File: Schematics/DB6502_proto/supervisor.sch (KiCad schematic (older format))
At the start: 33 parts, among them J4 AVR ISP, J5 Debug UART, J6 USB_B, U13 74AC74, U14 ATmega644PA-PU, U15 74HC595, U16 74HC157, U17 FT230XS, U5 74AC04, U7 74HC74, U8 74AC08, Y1 20MHz

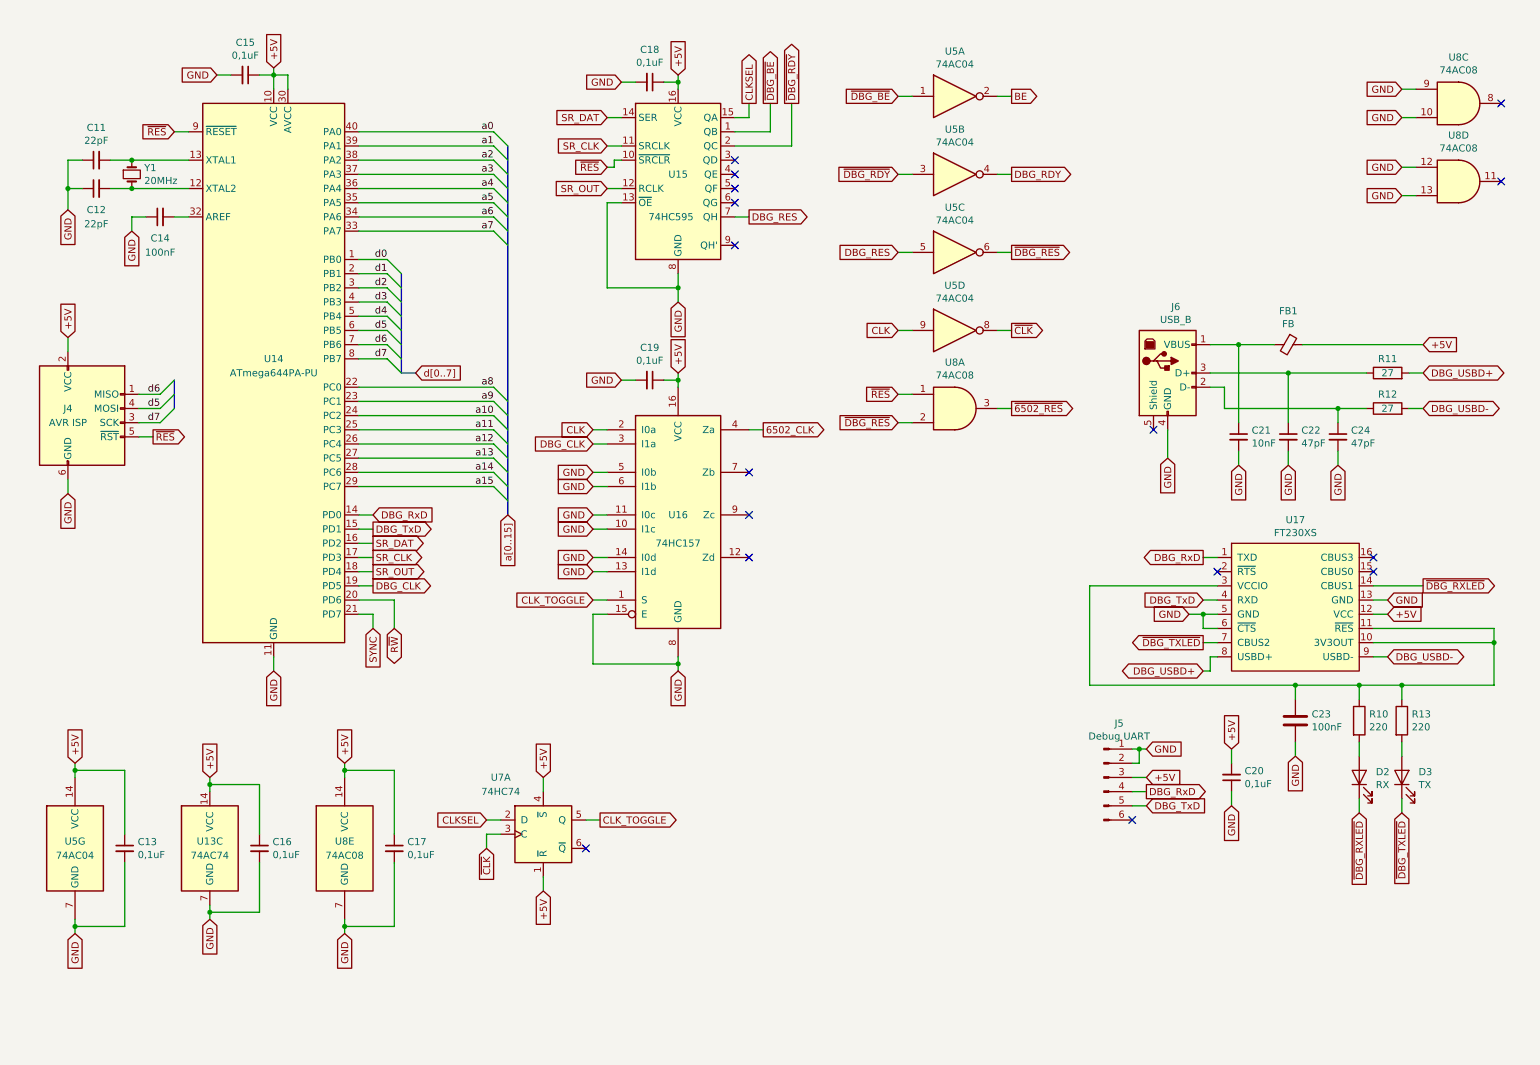
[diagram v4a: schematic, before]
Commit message: Implemented fix for metastability issue during clock switch
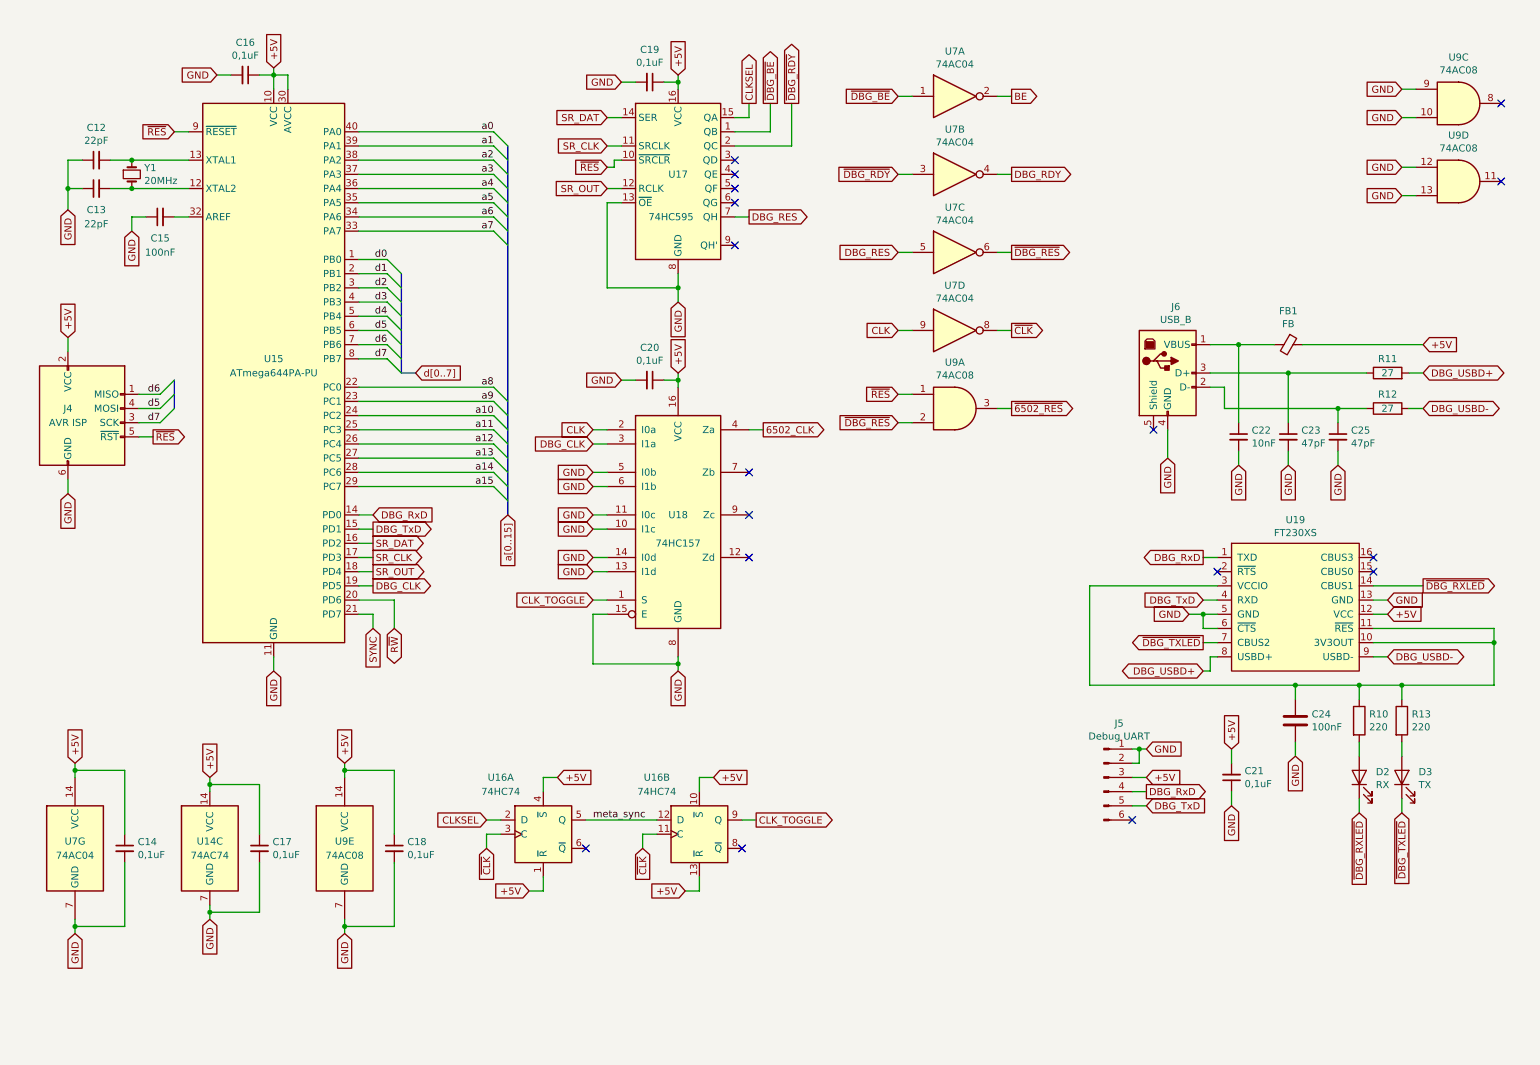
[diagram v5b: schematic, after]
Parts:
- added unit 2 of U16
- renumbered C11 to C12, C12 to C13, C13 to C14, C14 to C15, C15 to C16, C16 to C17, C17 to C18, C18 to C19, C19 to C20, C20 to C21, C21 to C22, C22 to C23, C23 to C24, C24 to C25, U13 to U14, U14 to U15, U7 to U16, U15 to U17, U16 to U18, U17 to U19, U5 to U7, U8 to U9
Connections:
- net +5V: now also U16.10 (~S), U16.13 (~R)
- net CLK_TOGGLE: now also U16.9 (Q); no longer U16.5 (Q)
- net ~CLK: now also U16.11 (C)
- new net meta_sync: U16.12 (D), U16.5 (Q)
- no-connect marks 16 -> 17
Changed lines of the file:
@@
 $EndComp
 $Comp
-L Device:C_Small C11
+L Device:C_Small C12
 U 1 1 5F942B94
 P 1050 1400
-F 0 "C11" V 1279 1400 50  0000 C CNN
+F 0 "C12" V 1279 1400 50  0000 C CNN
 F 1 "22pF" V 1188 1400 50  0000 C CNN
 F 2 "Capacitor_THT:C_Disc_D5.0mm_W2.5mm_P2.50mm" H 1050 1400 50  0001 C CNN
@@
 $EndComp
 $Comp
-L Device:C_Small C12
+L Device:C_Small C13
 U 1 1 5F942B9A
 P 1050 1600
-F 0 "C12" V 900 1600 50  0000 C CNN
+F 0 "C13" V 900 1600 50  0000 C CNN
 F 1 "22pF" V 800 1600 50  0000 C CNN
 F 2 "Capacitor_THT:C_Disc_D5.0mm_W2.5mm_P2.50mm" H 1050 1600 50  0001 C CNN
@@
 Connection ~ 1300 1600
 $Comp
-L Device:C_Small C14
+L Device:C_Small C15
 U 1 1 5F942BA9
 P 1500 1800
-F 0 "C14" V 1350 1800 50  0000 C CNN
+F 0 "C15" V 1350 1800 50  0000 C CNN
 F 1 "100nF" V 1250 1800 50  0000 C CNN
 F 2 "Capacitor_THT:C_Disc_D5.0mm_W2.5mm_P2.50mm" H 1500 1800 50  0001 C CNN
@@
 	850  1600 850  1750
 $Comp
-L MCU_Microchip_ATmega:ATmega644PA-PU U14
+L MCU_Microchip_ATmega:ATmega644PA-PU U15
 U 1 1 5F942C1A
 P 2300 2900
-F 0 "U14" H 2300 3000 50  0000 C CNN
+F 0 "U15" H 2300 3000 50  0000 C CNN
 F 1 "ATmega644PA-PU" H 2300 2900 50  0000 C CNN
 F 2 "Package_DIP:DIP-40_W15.24mm_Socket" H 2300 2900 50  0001 C CIN
@@
 P 9500 4550
 AR Path="/6014B4D9/5F9AD1D3" Ref="U?"  Part="1"
-AR Path="/5F8F4E1E/5F9AD1D3" Ref="U17"  Part="1"
-F 0 "U17" H 9500 5165 50  0000 C CNN
+AR Path="/5F8F4E1E/5F9AD1D3" Ref="U19"  Part="1"
+F 0 "U19" H 9500 5165 50  0000 C CNN
 F 1 "FT230XS" H 9500 5074 50  0000 C CNN
 F 2 "Package_SO:SSOP-16_5.3x6.2mm_P0.65mm" H 9500 5050 50  0001 C CNN
@@
 P 9500 5350
 AR Path="/6014B4D9/5F9AD1F3" Ref="C?"  Part="1"
-AR Path="/5F8F4E1E/5F9AD1F3" Ref="C23"  Part="1"
-F 0 "C23" H 9615 5396 50  0000 L CNN
+AR Path="/5F8F4E1E/5F9AD1F3" Ref="C24"  Part="1"
+F 0 "C24" H 9615 5396 50  0000 L CNN
 F 1 "100nF" H 9615 5305 50  0000 L CNN
 F 2 "Capacitor_THT:C_Disc_D5.0mm_W2.5mm_P2.50mm" H 9538 5200 50  0001 C CNN
@@
 P 9450 3350
 AR Path="/6014B4D9/5F9AD23C" Ref="C?"  Part="1"
-AR Path="/5F8F4E1E/5F9AD23C" Ref="C22"  Part="1"
-F 0 "C22" H 9542 3396 50  0000 L CNN
+AR Path="/5F8F4E1E/5F9AD23C" Ref="C23"  Part="1"
+F 0 "C23" H 9542 3396 50  0000 L CNN
 F 1 "47pF" H 9542 3305 50  0000 L CNN
 F 2 "Capacitor_THT:C_Disc_D5.0mm_W2.5mm_P2.50mm" H 9450 3350 50  0001 C CNN
@@
 P 9800 3350
 AR Path="/6014B4D9/5F9AD242" Ref="C?"  Part="1"
-AR Path="/5F8F4E1E/5F9AD242" Ref="C24"  Part="1"
-F 0 "C24" H 9892 3396 50  0000 L CNN
+AR Path="/5F8F4E1E/5F9AD242" Ref="C25"  Part="1"
+F 0 "C25" H 9892 3396 50  0000 L CNN
 F 1 "47pF" H 9892 3305 50  0000 L CNN
 F 2 "Capacitor_THT:C_Disc_D5.0mm_W2.5mm_P2.50mm" H 9800 3350 50  0001 C CNN
@@
 P 9100 3350
 AR Path="/6014B4D9/5F9AD254" Ref="C?"  Part="1"
-AR Path="/5F8F4E1E/5F9AD254" Ref="C21"  Part="1"
-F 0 "C21" H 9192 3396 50  0000 L CNN
+AR Path="/5F8F4E1E/5F9AD254" Ref="C22"  Part="1"
+F 0 "C22" H 9192 3396 50  0000 L CNN
 F 1 "10nF" H 9192 3305 50  0000 L CNN
 F 2 "Capacitor_THT:C_Disc_D5.0mm_W2.5mm_P2.50mm" H 9100 3350 50  0001 C CNN
@@
 	8450 5950 8350 5950
 $Comp
-L 74xx:74HC595 U15
+L 74xx:74HC595 U17
 U 1 1 5F9C2188
 P 5150 1500
-F 0 "U15" H 5150 1500 50  0000 C CNN
+F 0 "U17" H 5150 1500 50  0000 C CNN
 F 1 "74HC595" H 5100 1200 50  0000 C CNN
 F 2 "" H 5150 1500 50  0001 C CNN
@@
 NoConn ~ 5550 2000
 $Comp
-L 74xx:74LS04 U5
+L 74xx:74LS04 U7
 U 1 1 5F92D3FA
 P 7100 950
-F 0 "U5" H 7100 1267 50  0000 C CNN
+F 0 "U7" H 7100 1267 50  0000 C CNN
 F 1 "74AC04" H 7100 1176 50  0000 C CNN
 F 2 "" H 7100 950 50  0001 C CNN
@@
 	7400 950  7500 950
 $Comp
-L 74xx:74LS04 U5
+L 74xx:74LS04 U7
 U 2 1 5F93AD6D
 P 7100 1500
-F 0 "U5" H 7100 1817 50  0000 C CNN
+F 0 "U7" H 7100 1817 50  0000 C CNN
 F 1 "74AC04" H 7100 1726 50  0000 C CNN
 F 2 "" H 7100 1500 50  0001 C CNN
@@
 	7400 1500 7500 1500
 $Comp
-L 74xx:74LS04 U5
+L 74xx:74LS04 U7
 U 7 1 5F946300
 P 900 6250
-F 0 "U5" H 900 6300 50  0000 C CNN
+F 0 "U7" H 900 6300 50  0000 C CNN
 F 1 "74AC04" H 900 6200 50  0000 C CNN
 F 2 "" H 900 6250 50  0001 C CNN
@@
 	900  5650 900  5700
 $Comp
-L 74xx:74LS04 U5
+L 74xx:74LS04 U7
 U 3 1 5F95A89B
 P 7100 2050
-F 0 "U5" H 7100 2367 50  0000 C CNN
+F 0 "U7" H 7100 2367 50  0000 C CNN
 F 1 "74AC04" H 7100 2276 50  0000 C CNN
 F 2 "" H 7100 2050 50  0001 C CNN
@@
 $EndComp
 $Comp
-L 74xx:74LS04 U5
+L 74xx:74LS04 U7
 U 4 1 5F95B175
 P 7100 2600
-F 0 "U5" H 7100 2917 50  0000 C CNN
+F 0 "U7" H 7100 2917 50  0000 C CNN
 F 1 "74AC04" H 7100 2826 50  0000 C CNN
 F 2 "" H 7100 2600 50  0001 C CNN
@@
 	7400 2050 7500 2050
 $Comp
-L 74xx:74LS08 U8
+L 74xx:74LS08 U9
 U 1 1 5F991189
 P 7100 3150
-F 0 "U8" H 7100 3475 50  0000 C CNN
+F 0 "U9" H 7100 3475 50  0000 C CNN
 F 1 "74AC08" H 7100 3384 50  0000 C CNN
 F 2 "" H 7100 3150 50  0001 C CNN
@@
 	7500 3150 7400 3150
 $Comp
-L 74xx:74LS157 U16
+L 74xx:74LS157 U18
 U 1 1 5F9A90DC
 P 5150 3900
-F 0 "U16" H 5150 3900 50  0000 C CNN
+F 0 "U18" H 5150 3900 50  0000 C CNN
 F 1 "74HC157" H 5150 3700 50  0000 C CNN
 F 2 "" H 5150 3900 50  0001 C CNN
@@
 	7400 2600 7500 2600
 $Comp
-L 74xx:74HC74 U13
+L 74xx:74HC74 U14
 U 3 1 5FA1E8BB
 P 1850 6250
-F 0 "U13" H 1850 6300 50  0000 C CNN
+F 0 "U14" H 1850 6300 50  0000 C CNN
 F 1 "74AC74" H 1850 6200 50  0000 C CNN
 F 2 "" H 1850 6250 50  0001 C CNN
@@
 	1850 5750 1850 5800
 $Comp
-L 74xx:74HC74 U7
+L 74xx:74HC74 U16
 U 1 1 5FA3C995
 P 4200 6150
-F 0 "U7" H 3900 6550 50  0000 C CNN
+F 0 "U16" H 3900 6550 50  0000 C CNN
 F 1 "74HC74" H 3900 6450 50  0000 C CNN
 F 2 "" H 4200 6150 50  0001 C CNN
@@
 	3800 6050 3900 6050
 NoConn ~ 4500 6250
-Text GLabel 4200 5750 1    50   Input ~ 0
-+5V
-Text GLabel 4200 6550 3    50   Input ~ 0
+Text GLabel 4300 5750 2    50   Input ~ 0
++5V
+Text GLabel 4100 6550 0    50   Input ~ 0
 +5V
 Wire Wire Line
@@
 Wire Wire Line
 	4200 5750 4200 5850
-Text GLabel 4600 6050 2    50   Output ~ 0
+Text GLabel 5700 6050 2    50   Output ~ 0
 CLK_TOGGLE
 Wire Wire Line
-	4600 6050 4500 6050
+	5000 6050 4500 6050
 Text GLabel 4550 4500 0    50   Input ~ 0
 CLK_TOGGLE
@@
 	4550 4500 4650 4500
 $Comp
-L Device:C_Small C13
+L Device:C_Small C14
 U 1 1 5FAB56CF
 P 1250 6250
-F 0 "C13" H 1342 6296 50  0000 L CNN
+F 0 "C14" H 1342 6296 50  0000 L CNN
 F 1 "0,1uF" H 1342 6205 50  0000 L CNN
 F 2 "" H 1250 6250 50  0001 C CNN
@@
 $EndComp
 $Comp
-L Device:C_Small C16
+L Device:C_Small C17
 U 1 1 5FAB6000
 P 2200 6250
-F 0 "C16" H 2292 6296 50  0000 L CNN
+F 0 "C17" H 2292 6296 50  0000 L CNN
 F 1 "0,1uF" H 2292 6205 50  0000 L CNN
 F 2 "" H 2200 6250 50  0001 C CNN
@@
 	1850 5800 1850 5850
 $Comp
-L Device:C_Small C19
+L Device:C_Small C20
 U 1 1 5FAF8D14
 P 4950 2950
-F 0 "C19" V 4721 2950 50  0000 C CNN
+F 0 "C20" V 4721 2950 50  0000 C CNN
 F 1 "0,1uF" V 4812 2950 50  0000 C CNN
 F 2 "" H 4950 2950 50  0001 C CNN
@@
 	5150 2950 5150 3000
 $Comp
-L 74xx:74LS08 U8
+L 74xx:74LS08 U9
 U 5 1 5FB0D0DC
 P 2800 6250
-F 0 "U8" H 2800 6300 50  0000 C CNN
+F 0 "U9" H 2800 6300 50  0000 C CNN
 F 1 "74AC08" H 2800 6200 50  0000 C CNN
 F 2 "" H 2800 6250 50  0001 C CNN
@@
 GND
 $Comp
-L Device:C_Small C17
+L Device:C_Small C18
 U 1 1 5FB0F869
 P 3150 6250
-F 0 "C17" H 3242 6296 50  0000 L CNN
+F 0 "C18" H 3242 6296 50  0000 L CNN
 F 1 "0,1uF" H 3242 6205 50  0000 L CNN
 F 2 "" H 3150 6250 50  0001 C CNN
@@
 	2800 6800 2800 6850
 $Comp
-L Device:C_Small C15
+L Device:C_Small C16
 U 1 1 5FB3967F
 P 2100 800
-F 0 "C15" V 1871 800 50  0000 C CNN
+F 0 "C16" V 1871 800 50  0000 C CNN
 F 1 "0,1uF" V 1962 800 50  0000 C CNN
 F 2 "" H 2100 800 50  0001 C CNN
@@
 	2200 800  2300 800
 $Comp
-L Device:C_Small C18
+L Device:C_Small C19
 U 1 1 5FB5019A
 P 4950 850
-F 0 "C18" V 4721 850 50  0000 C CNN
+F 0 "C19" V 4721 850 50  0000 C CNN
 F 1 "0,1uF" V 4812 850 50  0000 C CNN
 F 2 "" H 4950 850 50  0001 C CNN
@@
 	5150 850  5150 900
 $Comp
-L 74xx:74LS08 U8
+L 74xx:74LS08 U9
 U 3 1 5FBB3E3E
 P 10650 1000
-F 0 "U8" H 10650 1325 50  0000 C CNN
+F 0 "U9" H 10650 1325 50  0000 C CNN
 F 1 "74AC08" H 10650 1234 50  0000 C CNN
 F 2 "" H 10650 1000 50  0001 C CNN
@@
 NoConn ~ 10950 1000
 $Comp
-L Device:C_Small C20
+L Device:C_Small C21
 U 1 1 5FC939BD
 P 9050 5750
-F 0 "C20" H 8958 5704 50  0000 R CNN
+F 0 "C21" H 8958 5704 50  0000 R CNN
 F 1 "0,1uF" H 8958 5795 50  0000 R CNN
 F 2 "" H 9050 5750 50  0001 C CNN
@@
 GND
 $Comp
-L 74xx:74LS08 U8
+L 74xx:74LS08 U9
 U 4 1 5FBB5F74
 P 10650 1550
-F 0 "U8" H 10650 1875 50  0000 C CNN
+F 0 "U9" H 10650 1875 50  0000 C CNN
 F 1 "74AC08" H 10650 1784 50  0000 C CNN
 F 2 "" H 10650 1550 50  0001 C CNN
@@
 Wire Wire Line
 	9550 2700 10400 2700
+$Comp
+L 74xx:74HC74 U16
+U 2 1 6000C6AE
+P 5300 6150
+F 0 "U16" H 5000 6550 50  0000 C CNN
+F 1 "74HC74" H 5000 6450 50  0000 C CNN
+F 2 "" H 5300 6150 50  0001 C CNN
+F 3 "74xx/74hc_hct74.pdf" H 5300 6150 50  0001 C CNN
+	2    5300 6150
+	1    0    0    -1
+$EndComp
+Text GLabel 4900 6250 3    50   Input ~ 0
+~CLK
+Wire Wire Line
+	4900 6250 4900 6150
+Wire Wire Line
+	4900 6150 5000 6150
+Wire Wire Line
+	4100 6550 4200 6550
+Wire Wire Line
+	4200 5750 4300 5750
+Text GLabel 5200 6550 0    50   Input ~ 0
++5V
+Wire Wire Line
+	5200 6550 5300 6550
+Wire Wire Line
+	5300 6550 5300 6450
+Text GLabel 5400 5750 2    50   Input ~ 0
++5V
+Wire Wire Line
+	5400 5750 5300 5750
+Wire Wire Line
+	5300 5750 5300 5850
+Wire Wire Line
+	5600 6050 5700 6050
+NoConn ~ 5600 6250
+Text Label 4550 6050 0    50   ~ 0
+meta_sync
 Wire Bus Line
 	1600 2950 1600 3150

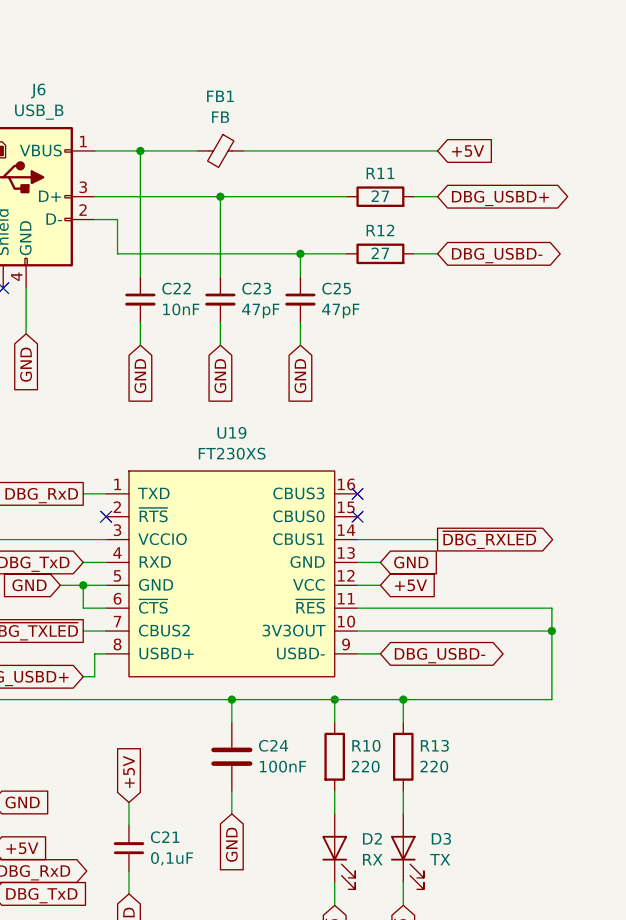
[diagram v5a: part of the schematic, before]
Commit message: Added jumpers for serial source selection
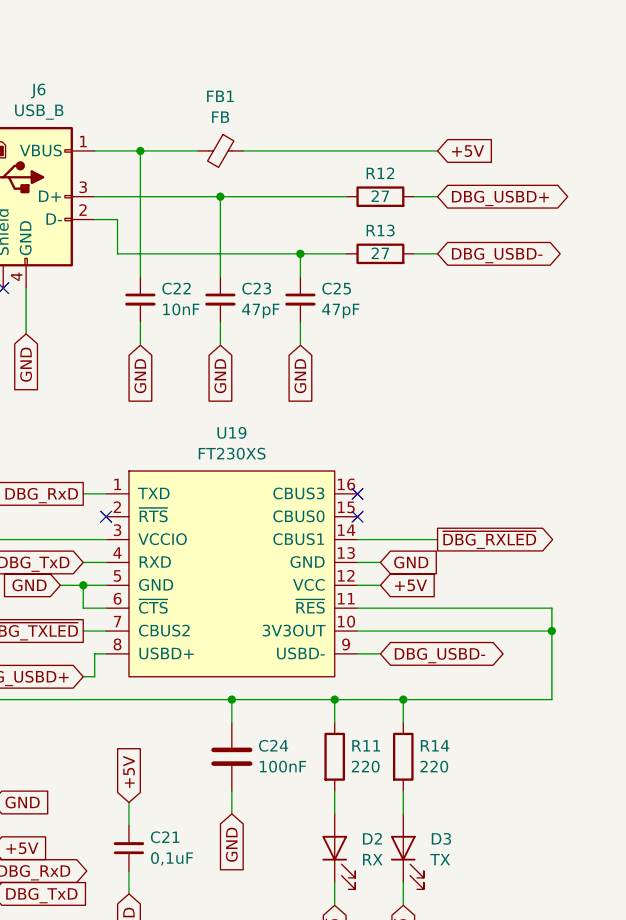
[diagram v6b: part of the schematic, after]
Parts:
- renumbered R10 to R11, R11 to R12, R12 to R13, R13 to R14
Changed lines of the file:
@@
 P 9950 5350
 AR Path="/6014B4D9/5F9AD207" Ref="R?"  Part="1"
-AR Path="/5F8F4E1E/5F9AD207" Ref="R10"  Part="1"
-F 0 "R10" H 10020 5396 50  0000 L CNN
+AR Path="/5F8F4E1E/5F9AD207" Ref="R11"  Part="1"
+F 0 "R11" H 10020 5396 50  0000 L CNN
 F 1 "220" H 10020 5305 50  0000 L CNN
 F 2 "Resistor_THT:R_Axial_DIN0207_L6.3mm_D2.5mm_P10.16mm_Horizontal" V 9880 5350 50  0001 C CNN
@@
 P 10250 5350
 AR Path="/6014B4D9/5F9AD20D" Ref="R?"  Part="1"
-AR Path="/5F8F4E1E/5F9AD20D" Ref="R13"  Part="1"
-F 0 "R13" H 10320 5396 50  0000 L CNN
+AR Path="/5F8F4E1E/5F9AD20D" Ref="R14"  Part="1"
+F 0 "R14" H 10320 5396 50  0000 L CNN
 F 1 "220" H 10320 5305 50  0000 L CNN
 F 2 "Resistor_THT:R_Axial_DIN0207_L6.3mm_D2.5mm_P10.16mm_Horizontal" V 10180 5350 50  0001 C CNN
@@
 P 10150 3150
 AR Path="/6014B4D9/5F9AD22D" Ref="R?"  Part="1"
-AR Path="/5F8F4E1E/5F9AD22D" Ref="R12"  Part="1"
-F 0 "R12" V 10250 3150 50  0000 C CNN
+AR Path="/5F8F4E1E/5F9AD22D" Ref="R13"  Part="1"
+F 0 "R13" V 10250 3150 50  0000 C CNN
 F 1 "27" V 10150 3150 50  0000 C CNN
 F 2 "Resistor_THT:R_Axial_DIN0207_L6.3mm_D2.5mm_P10.16mm_Horizontal" V 10080 3150 50  0001 C CNN
@@
 P 10150 2900
 AR Path="/6014B4D9/5F9AD233" Ref="R?"  Part="1"
-AR Path="/5F8F4E1E/5F9AD233" Ref="R11"  Part="1"
-F 0 "R11" V 10250 2900 50  0000 C CNN
+AR Path="/5F8F4E1E/5F9AD233" Ref="R12"  Part="1"
+F 0 "R12" V 10250 2900 50  0000 C CNN
 F 1 "27" V 10150 2900 50  0000 C CNN
 F 2 "Resistor_THT:R_Axial_DIN0207_L6.3mm_D2.5mm_P10.16mm_Horizontal" V 10080 2900 50  0001 C CNN
